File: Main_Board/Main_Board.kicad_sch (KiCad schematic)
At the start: 1 part, among them U1 OKI-78SR-3.3_1.5-W36-C

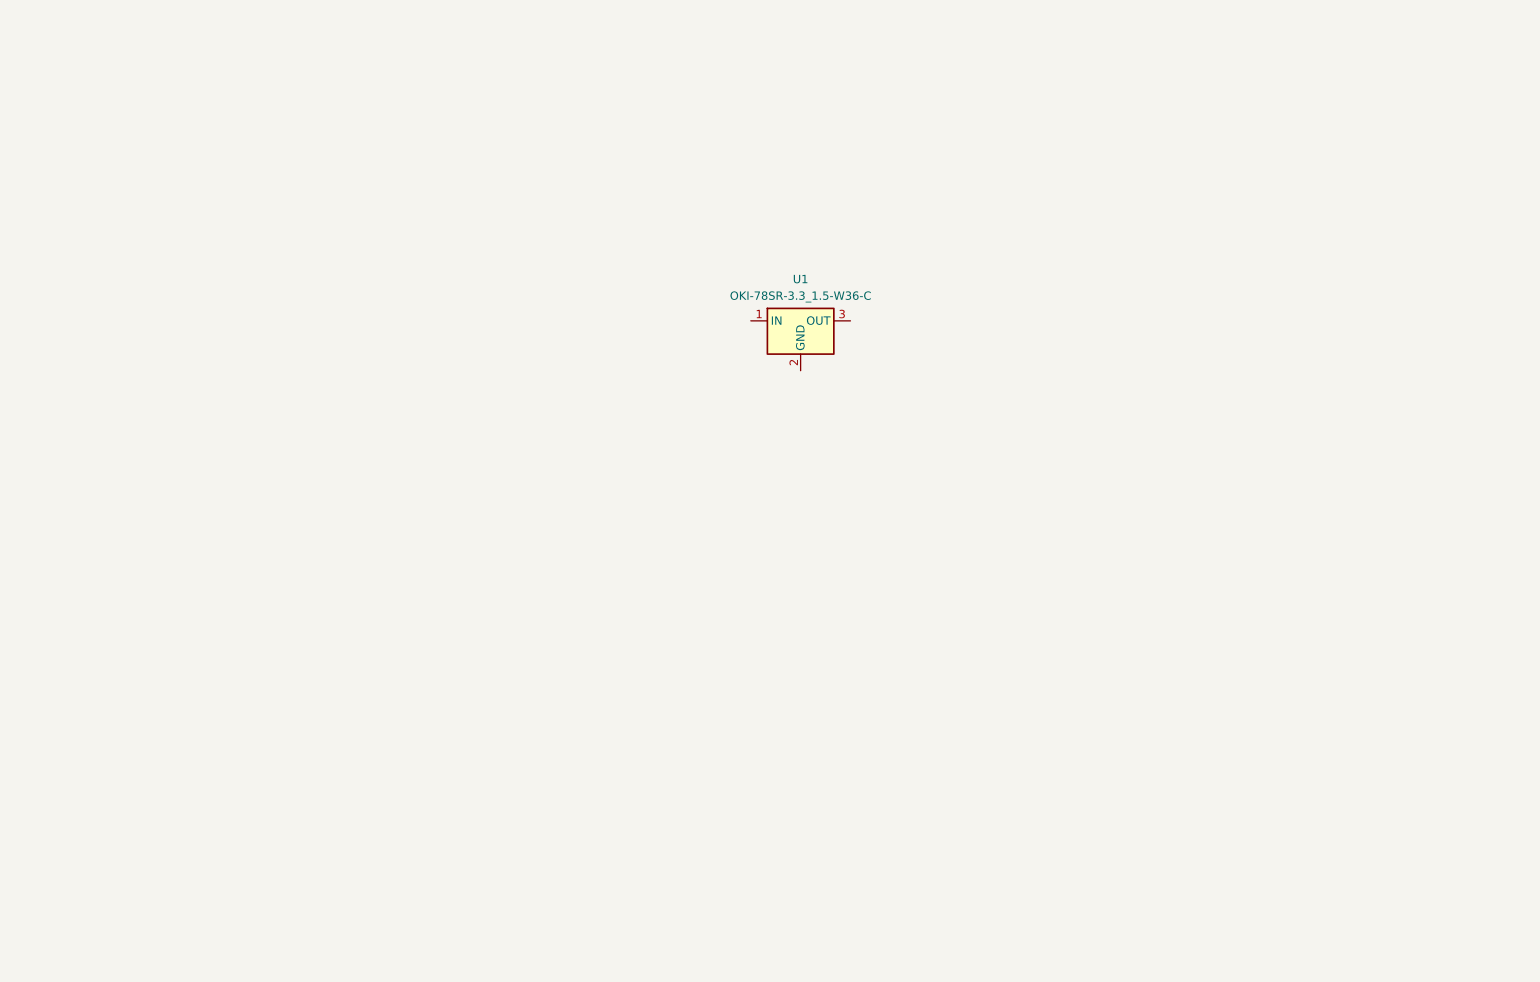
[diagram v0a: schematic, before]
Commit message: Buck Teensy Can Transciever
I added some basic circuits. We need to regulate the voltage around the ground on the buck converter.
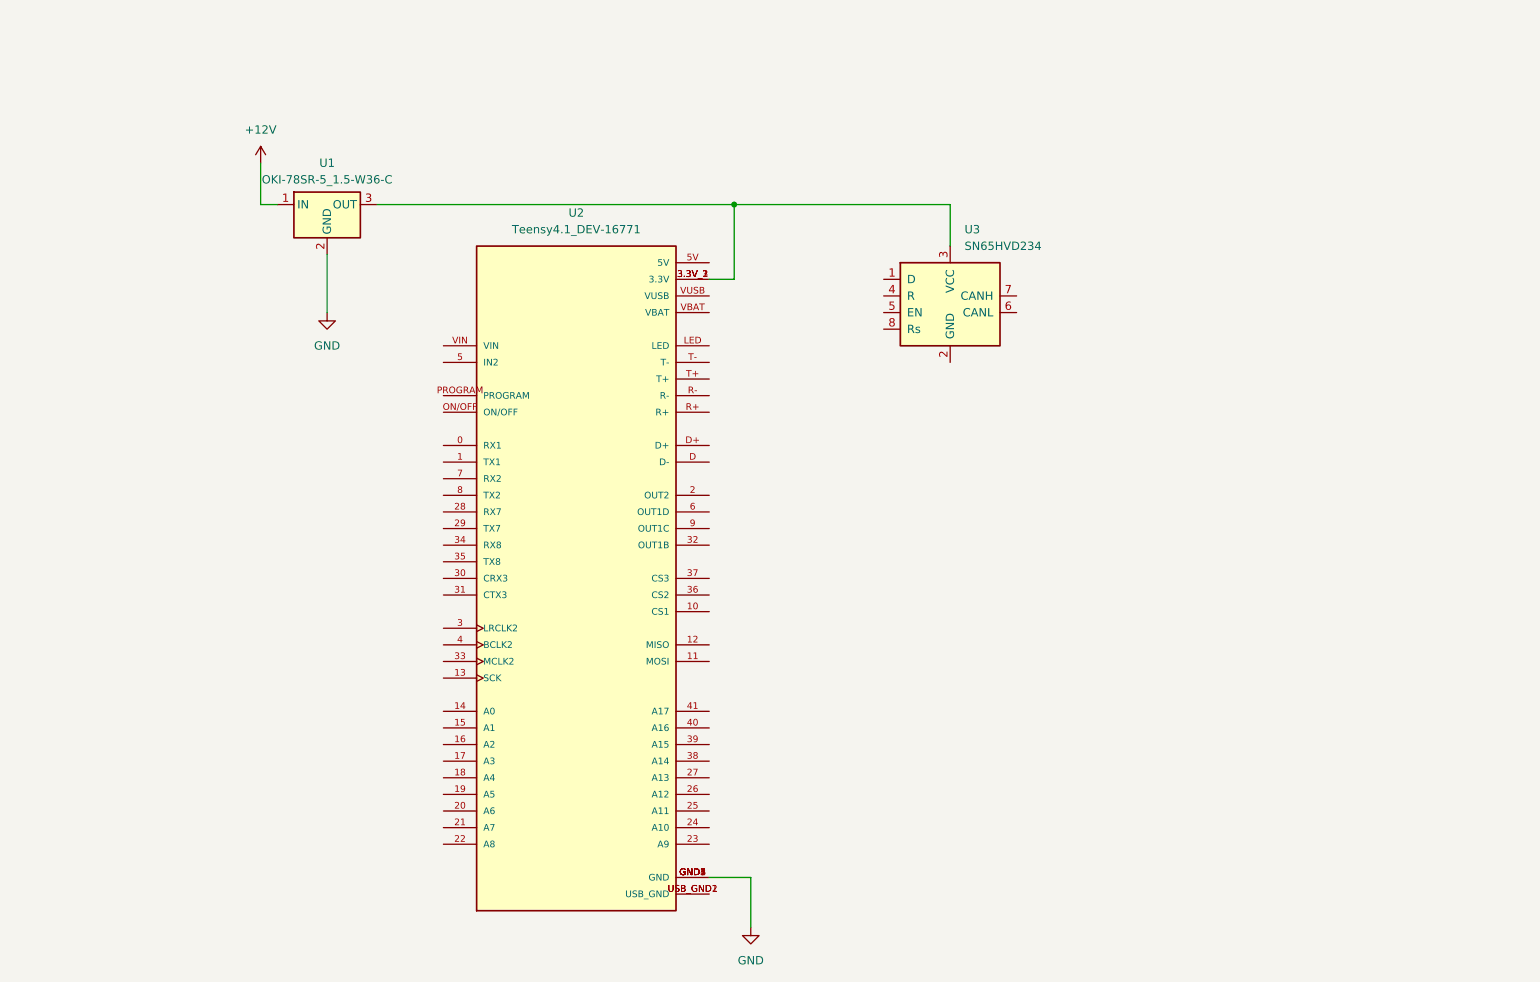
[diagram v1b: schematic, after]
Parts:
- removed U1: OKI-78SR-3.3_1.5-W36-C, Converter_DCDC:Converter_DCDC_Murata_OKI-78SR_Vertical, symbol Converter_DCDC:OKI-78SR-3.3_1.5-W36-C
- added U1: OKI-78SR-5_1.5-W36-C, Converter_DCDC:Converter_DCDC_Murata_OKI-78SR_Vertical, symbol Converter_DCDC:OKI-78SR-5_1.5-W36-C
- added U2: Teensy4.1_DEV-16771, MODULE_DEV-16771, symbol MRDT_Shields:Teensy4.1_DEV-16771
- added U3: SN65HVD234, Package_SO:SOIC-8_3.9x4.9mm_P1.27mm, symbol Interface_CAN_LIN:SN65HVD234
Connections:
- new net: U1.3 (OUT), U2.3.3V_1 (3.3V), U2.3.3V_2 (3.3V), U2.3.3V_3 (3.3V), U3.3 (VCC)
- new net: U2.USB_GND1 (USB_GND), U2.USB_GND2 (USB_GND)
- new net +12V: U1.1 (IN)
- new net GND: U1.2 (GND), U2.GND1 (GND), U2.GND2 (GND), U2.GND3 (GND), U2.GND4 (GND), U2.GND5 (GND)

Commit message: Buck converter design is finalized
Fixed the buck converter so the output voltage is constant.

To Work On:
-Work on transceiver (Talk to Adam)
-Add some inputs for encoders
-Add some inputs for heat sensors
-Find a datasheet and capacitor for the 100nf and 1nf capacitors.
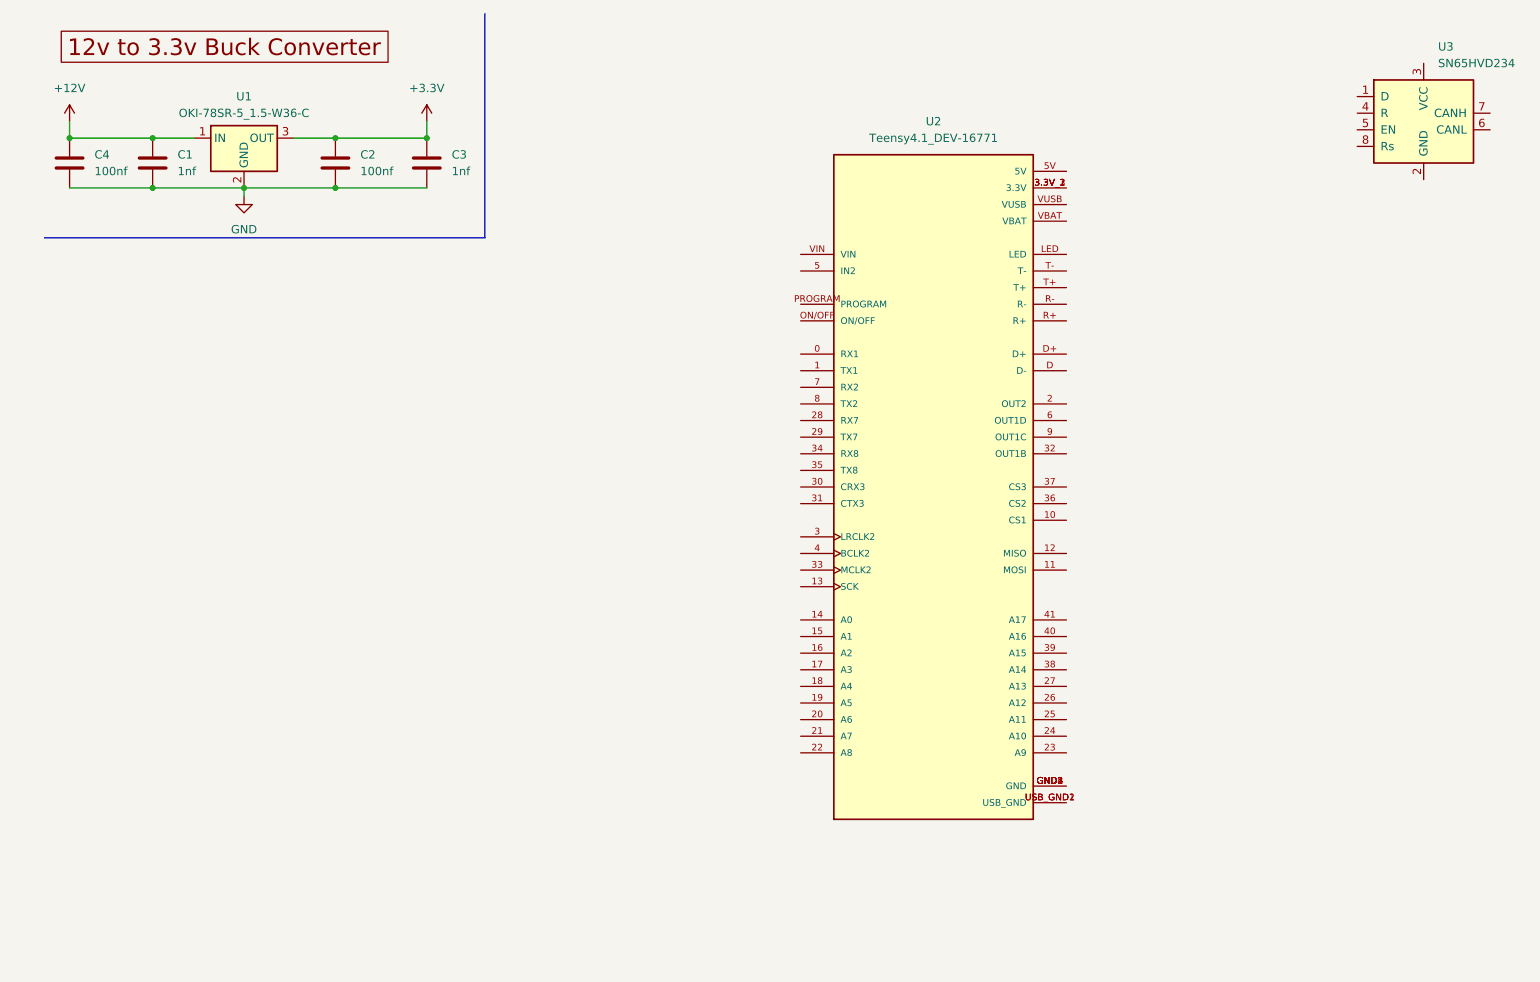
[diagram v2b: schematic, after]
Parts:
- added C1, C3: 1nf, symbol Device:C
- added C2, C4: 100nf, symbol Device:C
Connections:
- net +12V: now also C1.1, C4.1
- net GND: now also C1.2, C2.2, C3.2, C4.2; no longer U2.GND1 (GND), U2.GND2 (GND), U2.GND3 (GND), U2.GND4 (GND), U2.GND5 (GND)
- net at U2.3.3V_1 (3.3V), U2.3.3V_2 (3.3V), U2.3.3V_3 (3.3V): no longer U1.3 (OUT), U3.3 (VCC)
- new net: U2.GND1 (GND), U2.GND2 (GND), U2.GND3 (GND), U2.GND4 (GND), U2.GND5 (GND)
- new net +3.3V: C2.1, C3.1, U1.3 (OUT)
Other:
- company: (none) -> MRDT
- title: (none) -> Brushless Arm Tester Board
- moved on the sheet: U1, U2, U3

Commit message: Added Voltage Inputs For Teensy
Trying to figure out how to hook up the CAN transceiver. And add the symbol.
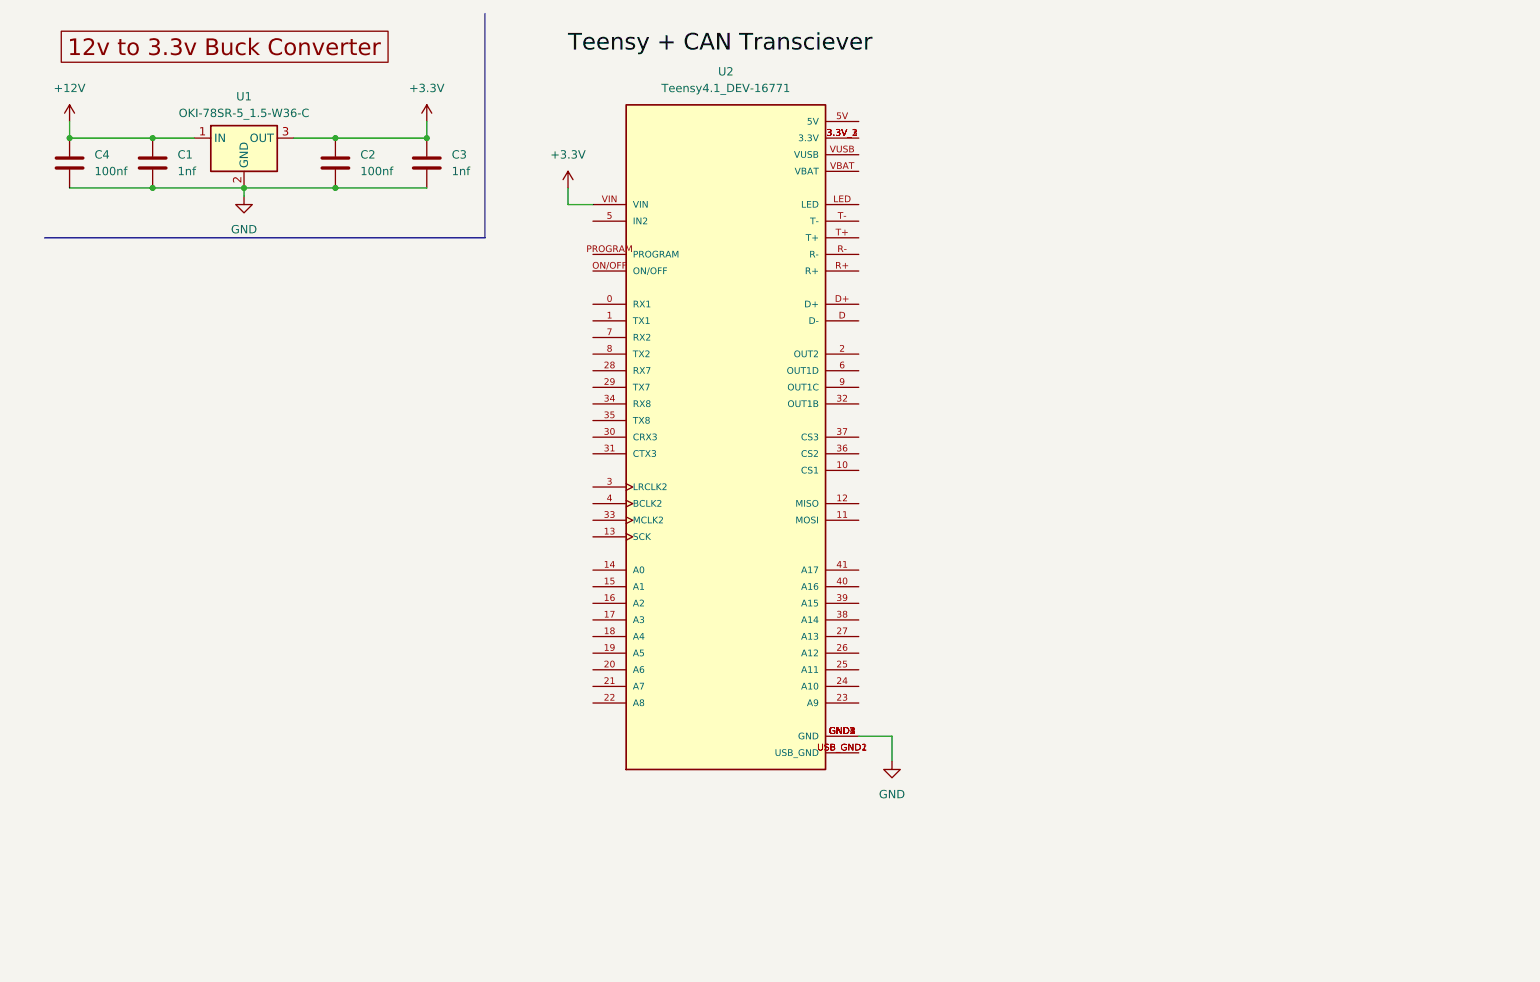
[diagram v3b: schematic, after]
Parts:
- removed U3: SN65HVD234, Package_SO:SOIC-8_3.9x4.9mm_P1.27mm, symbol Interface_CAN_LIN:SN65HVD234
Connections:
- net +3.3V: now also U2.VIN
- net GND: now also U2.GND1 (GND), U2.GND2 (GND), U2.GND3 (GND), U2.GND4 (GND), U2.GND5 (GND)
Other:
- moved on the sheet: U2
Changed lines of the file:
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@@
+	(wire
+		(pts
+			(xy 142.24 123.19) (xy 137.16 123.19)
+		)
+		(stroke
+			(width 0)
+			(type default)
+		)
+	)
 	(wire
 		(pts
@@
 		(pts
 			(xy 43.18 39.37) (xy 57.15 39.37)
+		)
+		(stroke
+			(width 0)
+			(type default)
+		)
+	)
+	(wire
+		(pts
+			(xy 92.71 41.91) (xy 92.71 39.37)
 		)
 		(stroke
@@
 	(wire
 		(pts
+			(xy 142.24 127) (xy 142.24 123.19)
+		)
+		(stroke
+			(width 0)
+			(type default)
+		)
+	)
+	(wire
+		(pts
 			(xy 16.51 29.21) (xy 16.51 31.75)
+		)
+		(stroke
+			(width 0)
+			(type default)
+		)
+	)
+	(wire
+		(pts
+			(xy 96.52 41.91) (xy 92.71 41.91)
 		)
 		(stroke
@@
 		)
 	)
+	(label "Teensy + CAN Transciever"
+		(at 92.71 19.05 0)
+		(fields_autoplaced yes)
+		(effects
+			(font
+				(size 2.54 2.54)
+			)
+			(justify left bottom)
+		)
+		(property "Netclass" "Teensy + CAN Transciever"
+			(at 92.71 20.955 0)
+			(effects
+				(font
+					(size 1.27 1.27)
+					(italic yes)
+				)
+				(justify left)
+				(hide yes)
+			)
+		)
+	)
 	(global_label "12v to 3.3v Buck Converter"
 		(shape passive)
@@
 				(justify left)
 				(hide yes)
+			)
+		)
+	)
+	(symbol
+		(lib_id "power:+3.3V")
+		(at 92.71 39.37 0)
+		(unit 1)
+		(exclude_from_sim no)
+		(in_bom yes)
+		(on_board yes)
+		(dnp no)
+		(fields_autoplaced yes)
+		(property "Reference" "#PWR04"
+			(at 92.71 43.18 0)
+			(effects
+				(font
+					(size 1.27 1.27)
+				)
+				(hide yes)
+			)
+		)
+		(property "Value" "+3.3V"
+			(at 92.71 34.29 0)
+			(effects
+				(font
+					(size 1.27 1.27)
+				)
+			)
+		)
+		(property "Footprint" ""
+			(at 92.71 39.37 0)
+			(effects
+				(font
+					(size 1.27 1.27)
+				)
+				(hide yes)
+			)
+		)
+		(property "Datasheet" ""
+			(at 92.71 39.37 0)
+			(effects
+				(font
+					(size 1.27 1.27)
+				)
+				(hide yes)
+			)
+		)
+		(property "Description" "Power symbol creates a global label with name \"+3.3V\""
+			(at 92.71 39.37 0)
+			(effects
+				(font
+					(size 1.27 1.27)
+				)
+				(hide yes)
+			)
+		)
+		(pin "1"
+		)
+		(instances
+			(project ""
+				(path "/7e76cf6a-e9a4-4ef3-bf05-f0b14a5efcef"
+					(reference "#PWR04")
+					(unit 1)
+				)
 			)
 		)
@@
 	(symbol
 		(lib_id "MRDT_Shields:Teensy4.1_DEV-16771")
-		(at 148.59 85.09 0)
+		(at 116.84 77.47 0)
 		(unit 1)
 		(exclude_from_sim no)
@@
 		(fields_autoplaced yes)
 		(property "Reference" "U2"
-			(at 148.59 29.21 0)
+			(at 116.84 21.59 0)
 			(effects
 				(font
@@
 		)
 		(property "Value" "Teensy4.1_DEV-16771"
-			(at 148.59 31.75 0)
+			(at 116.84 24.13 0)
 			(effects
 				(font
@@
 		)
 		(property "Footprint" "MODULE_DEV-16771"
-			(at 201.93 92.71 0)
+			(at 170.18 85.09 0)
 			(effects
 				(font
@@
 		)
 		(property "Datasheet" ""
-			(at 148.59 85.09 0)
+			(at 116.84 77.47 0)
 			(effects
 				(font
@@
 		)
 		(property "Description" ""
-			(at 148.59 85.09 0)
+			(at 116.84 77.47 0)
 			(effects
 				(font
@@
 		)
 		(property "STANDARD" "Manufacturer recommendations"
-			(at 201.93 99.06 0)
+			(at 170.18 91.44 0)
 			(effects
 				(font
@@
 		)
 		(property "MAXIMUM_PACKAGE_HEIGHT" "4.07mm"
-			(at 208.28 104.14 0)
+			(at 176.53 96.52 0)
 			(effects
 				(font
@@
 		)
 		(property "MANUFACTURER" "SparkFun Electronics"
-			(at 207.01 107.95 0)
+			(at 175.26 100.33 0)
 			(effects
 				(font
@@
 		)
 		(property "PARTREV" "4.1"
-			(at 140.97 140.97 0)
+			(at 109.22 133.35 0)
 			(effects
 				(font
@@
 	)
 	(symbol
-		(lib_id "Interface_CAN_LIN:SN65HVD234")
-		(at 223.52 27.94 0)
-		(unit 1)
-		(exclude_from_sim no)
-		(in_bom yes)
-		(on_board yes)
-		(dnp no)
-		(fields_autoplaced yes)
-		(property "Reference" "U3"
-			(at 225.7141 17.78 0)
-			(effects
-				(font
-					(size 1.27 1.27)
-				)
-				(justify left)
-			)
-		)
-		(property "Value" "SN65HVD234"
-			(at 225.7141 20.32 0)
-			(effects
-				(font
-					(size 1.27 1.27)
-				)
-				(justify left)
-			)
-		)
-		(property "Footprint" "Package_SO:SOIC-8_3.9x4.9mm_P1.27mm"
-			(at 223.52 40.64 0)
-			(effects
-				(font
-					(size 1.27 1.27)
-				)
-				(hide yes)
-			)
-		)
-		(property "Datasheet" "http://www.ti.com/lit/ds/symlink/sn65hvd234.pdf"
-			(at 220.98 17.78 0)
-			(effects
-				(font
-					(size 1.27 1.27)
-				)
-				(hide yes)
-			)
-		)
-		(property "Description" "CAN Bus Transceiver, 3.3V, 1Mbps, Enable feature, SOIC-8"
-			(at 223.52 27.94 0)
-			(effects
-				(font
-					(size 1.27 1.27)
-				)
-				(hide yes)
-			)
-		)
-		(pin "8"
-		)
-		(pin "1"
-		)
-		(pin "3"
-		)
-		(pin "5"
-		)
-		(pin "7"
-		)
-		(pin "4"
-		)
-		(pin "2"
-		)
-		(pin "6"
-		)
-		(instances
-			(project "Main_Board"
-				(path "/7e76cf6a-e9a4-4ef3-bf05-f0b14a5efcef"
-					(reference "U3")
-					(unit 1)
-				)
-			)
-		)
-	)
-	(symbol
 		(lib_id "power:+12V")
 		(at 16.51 29.21 0)
@@
 					(unit 1)
 				)
+			)
+		)
+	)
+	(symbol
+		(lib_id "power:GND")
+		(at 142.24 127 0)
+		(unit 1)
+		(exclude_from_sim no)
+		(in_bom yes)
+		(on_board yes)
+		(dnp no)
+		(fields_autoplaced yes)
+		(property "Reference" "#PWR05"
+			(at 142.24 133.35 0)
+			(effects
+				(font
+					(size 1.27 1.27)
+				)
+				(hide yes)
+			)
+		)
+		(property "Value" "GND"
+			(at 142.24 132.08 0)
+			(effects
+				(font
+					(size 1.27 1.27)
+				)
+			)
+		)
+		(property "Footprint" ""
+			(at 142.24 127 0)
+			(effects
+				(font
+					(size 1.27 1.27)
+				)
+				(hide yes)
+			)
+		)
+		(property "Datasheet" ""
+			(at 142.24 127 0)
+			(effects
+				(font
+					(size 1.27 1.27)
+				)
+				(hide yes)
+			)
+		)
+		(property "Description" "Power symbol creates a global label with name \"GND\" , ground"
+			(at 142.24 127 0)
+			(effects
+				(font
+					(size 1.27 1.27)
+				)
+				(hide yes)
+			)
+		)
+		(pin "1"
+		)
+		(instances
+			(project ""
+				(path "/7e76cf6a-e9a4-4ef3-bf05-f0b14a5efcef"
+					(reference "#PWR05")
+					(unit 1)
+				)
